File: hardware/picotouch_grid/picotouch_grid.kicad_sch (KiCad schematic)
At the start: 164 parts, among them J1 TRRS, J2 TRRS, J3 TRRS, U1 Pico, U2 TS20, U3 TS20, U5 H11L1

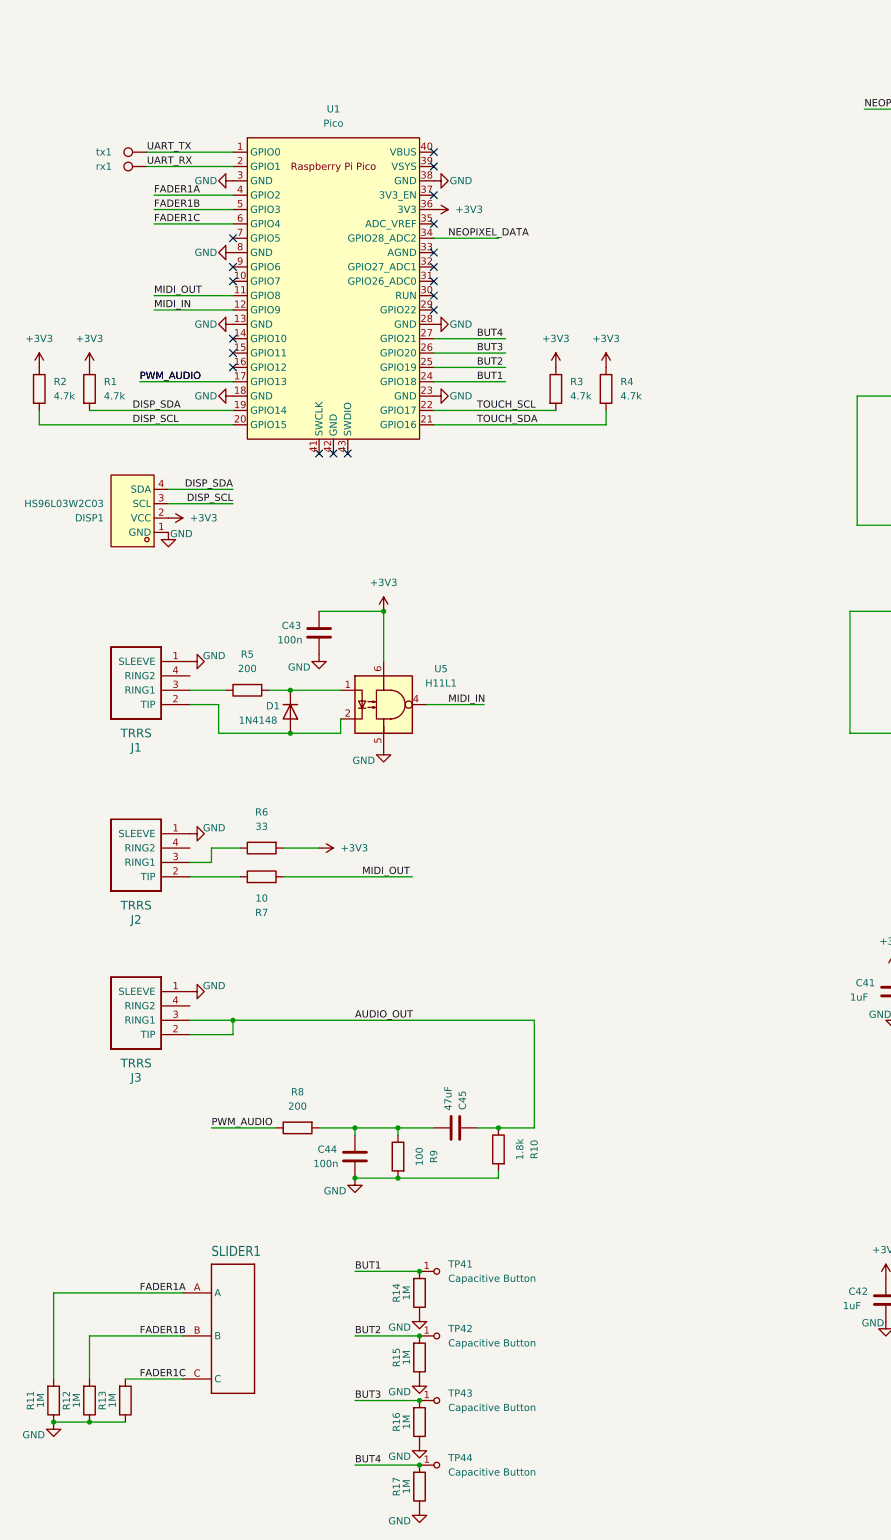
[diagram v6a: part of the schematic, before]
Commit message: pcb: another fader, i2c trace reorg
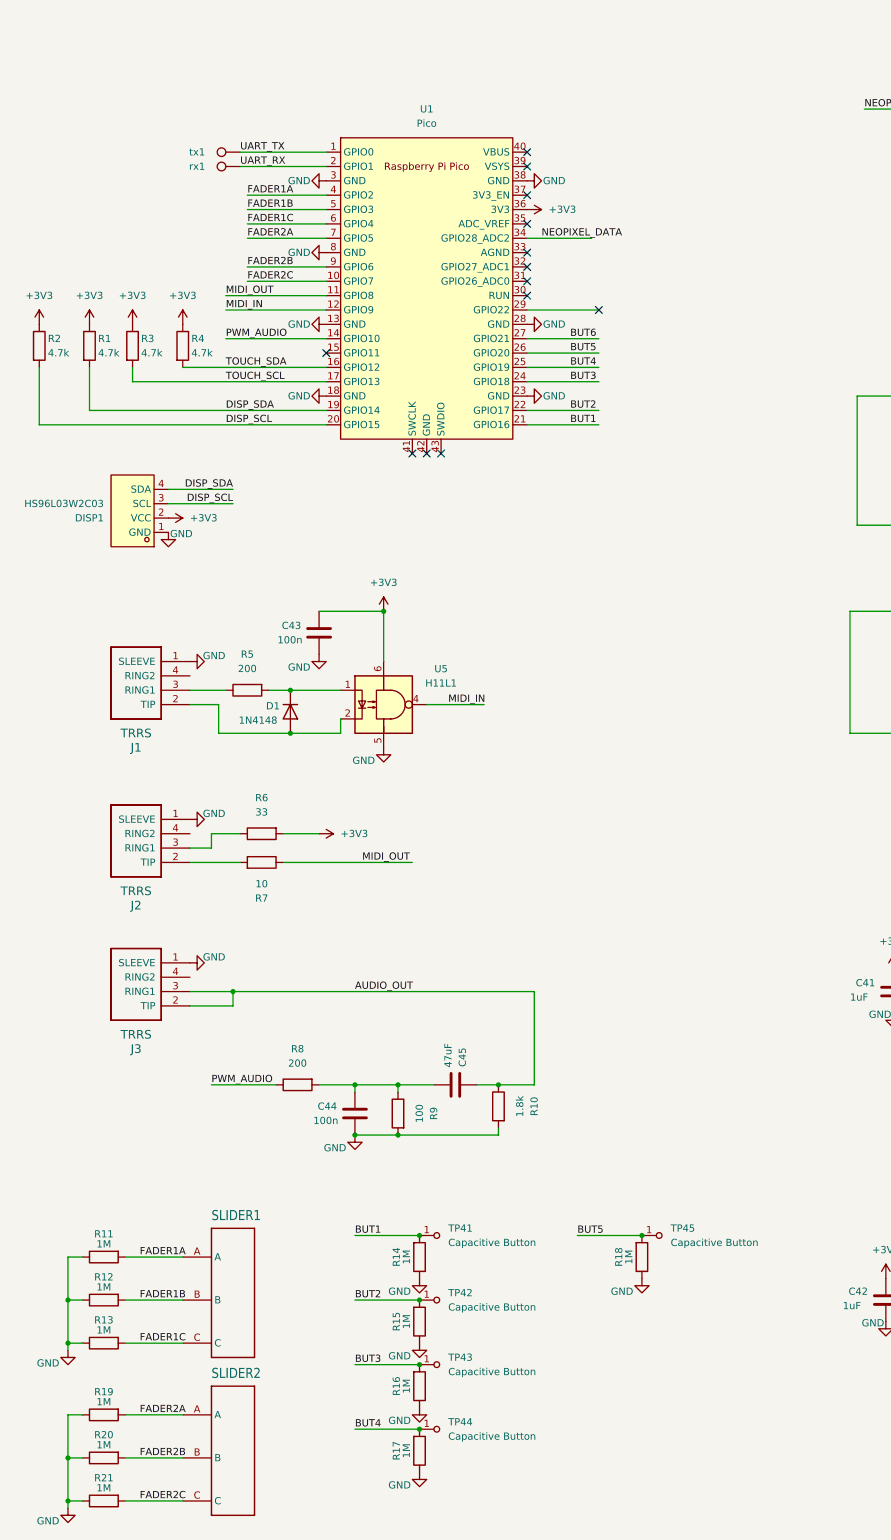
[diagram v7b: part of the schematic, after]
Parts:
- added R18, R19, R20, R21: 1M, Resistor_SMD:R_0603_1608Metric, symbol Device:R
- added SLIDER2: ~, todbot_eagle2023:TOUCHSLIDER3_8x40B, symbol todbot_eagle2023:TouchSlider-3sectors
- added TP45: Capacitive Button, todbot_stuff:Pad-CapacitiveTouch-SparkFun-10x5mm-roundrect, symbol SparkFun-Switch:Capacitive Button
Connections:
- net BUT1: now also U1.21 (GPIO16); no longer U1.24 (GPIO18)
- net BUT2: now also U1.22 (GPIO17); no longer U1.25 (GPIO19)
- net BUT3: now also U1.24 (GPIO18); no longer U1.26 (GPIO20)
- net BUT4: now also U1.25 (GPIO19); no longer U1.27 (GPIO21)
- net GND: now also R18.1, R19.1, R20.1, R21.1
- net PWM_AUDIO: now also U1.14 (GPIO10); no longer U1.17 (GPIO13)
- net TOUCH_SCL: now also U1.17 (GPIO13); no longer U1.22 (GPIO17)
- net TOUCH_SDA: now also U1.16 (GPIO12); no longer U1.21 (GPIO16)
- net FADER2C: now reaches U1.10 (GPIO7)
- net FADER2C: now also R21.2, SLIDER2.C
- net FADER2A: now reaches U1.7 (GPIO5)
- net FADER2A: now also R19.2, SLIDER2.A
- net FADER2B: now reaches U1.9 (GPIO6)
- net FADER2B: now also R20.2, SLIDER2.B
- new net BUT5: R18.2, TP45.1 (A), U1.26 (GPIO20)
- new net BUT6: U1.27 (GPIO21)
- no-connect marks 21 -> 16
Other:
- moved on the sheet: C44, C45, J2, J3, R1, R10, R11, R12, R13, R14, R15, R16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

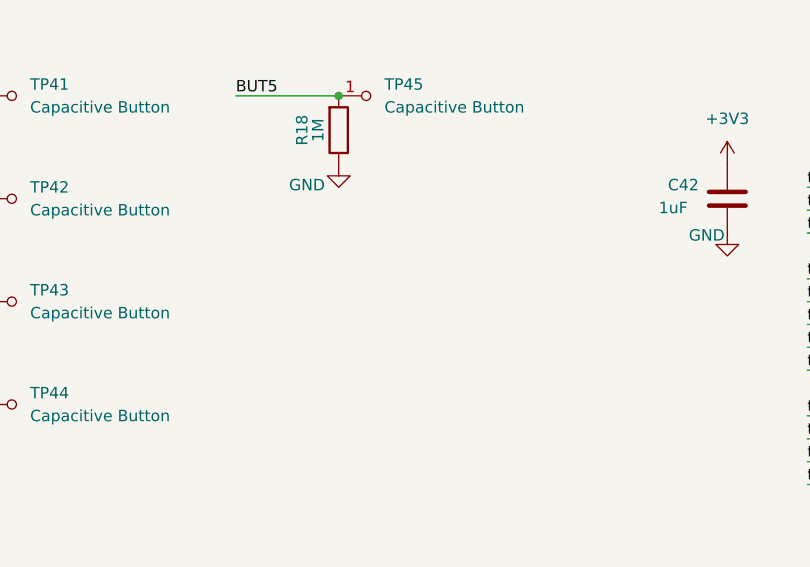
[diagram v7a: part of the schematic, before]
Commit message: pcb: button layout tune
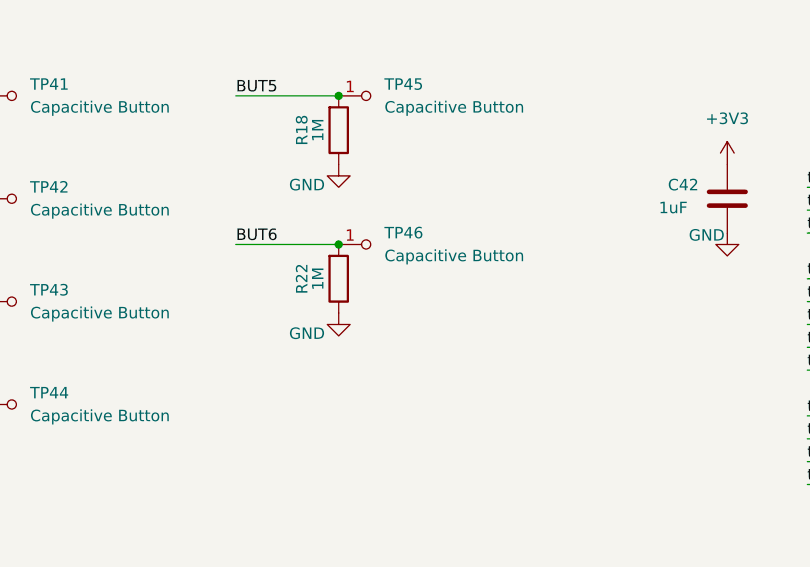
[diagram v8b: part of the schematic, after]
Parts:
- added R22: 1M, Resistor_SMD:R_0603_1608Metric, symbol Device:R
- added TP46: Capacitive Button, todbot_stuff:Pad-CapacitiveTouch-SparkFun-10x5mm-roundrect, symbol SparkFun-Switch:Capacitive Button
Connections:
- net BUT6: now also R22.2, TP46.1 (A)
- net GND: now also R22.1
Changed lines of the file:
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@@
 	)
 	(junction
+		(at 124.46 247.65)
+		(diameter 0)
+		(color 0 0 0 0)
+	)
+	(junction
 		(at 325.12 92.71)
 		(diameter 0)
@@
 	(wire
 		(pts
+			(xy 113.03 247.65) (xy 124.46 247.65)
+		)
+		(stroke
+			(width 0)
+			(type default)
+		)
+	)
+	(wire
+		(pts
 			(xy 271.78 55.88) (xy 279.4 55.88)
 		)
@@
 		)
 	)
+	(label "BUT6"
+		(at 113.03 247.65 0)
+		(fields_autoplaced yes)
+		(effects
+			(font
+				(size 1.27 1.27)
+			)
+			(justify left bottom)
+		)
+	)
 	(label "tp35"
 		(at 367.03 203.2 0)
@@
 	)
 	(symbol
+		(lib_id "power:GND")
+		(at 124.46 255.27 0)
+		(unit 1)
+		(exclude_from_sim no)
+		(in_bom yes)
+		(on_board yes)
+		(dnp no)
+		(property "Reference" "#PWR0164"
+			(at 124.46 261.62 0)
+			(effects
+				(font
+					(size 1.27 1.27)
+				)
+				(hide yes)
+			)
+		)
+		(property "Value" "GND"
+			(at 122.936 257.556 0)
+			(effects
+				(font
+					(size 1.27 1.27)
+				)
+				(justify right)
+			)
+		)
+		(property "Footprint" ""
+			(at 124.46 255.27 0)
+			(effects
+				(font
+					(size 1.27 1.27)
+				)
+				(hide yes)
+			)
+		)
+		(property "Datasheet" ""
+			(at 124.46 255.27 0)
+			(effects
+				(font
+					(size 1.27 1.27)
+				)
+				(hide yes)
+			)
+		)
+		(property "Description" "Power symbol creates a global label with name \"GND\" , ground"
+			(at 124.46 255.27 0)
+			(effects
+				(font
+					(size 1.27 1.27)
+				)
+				(hide yes)
+			)
+		)
+		(pin "1"
+		)
+		(instances
+			(project "picotouch_grid"
+				(path "/036e8f10-ba17-4cdc-95e8-e722ded3fffe"
+					(reference "#PWR0164")
+					(unit 1)
+				)
+			)
+		)
+	)
+	(symbol
 		(lib_id "PCM_marbastlib-various:SK6812MINI-E")
 		(at 325.12 31.75 0)
@@
 	(symbol
 		(lib_id "Device:R")
+		(at 124.46 251.46 0)
+		(mirror x)
+		(unit 1)
+		(exclude_from_sim no)
+		(in_bom yes)
+		(on_board yes)
+		(dnp no)
+		(property "Reference" "R22"
+			(at 120.396 251.46 90)
+			(effects
+				(font
+					(size 1.27 1.27)
+				)
+			)
+		)
+		(property "Value" "1M"
+			(at 122.174 251.46 90)
+			(effects
+				(font
+					(size 1.27 1.27)
+				)
+			)
+		)
+		(property "Footprint" "Resistor_SMD:R_0603_1608Metric"
+			(at 122.682 251.46 90)
+			(effects
+				(font
+					(size 1.27 1.27)
+				)
+				(hide yes)
+			)
+		)
+		(property "Datasheet" "~"
+			(at 124.46 251.46 0)
+			(effects
+				(font
+					(size 1.27 1.27)
+				)
+				(hide yes)
+			)
+		)
+		(property "Description" "Resistor"
+			(at 124.46 251.46 0)
+			(effects
+				(font
+					(size 1.27 1.27)
+				)
+				(hide yes)
+			)
+		)
+		(pin "2"
+		)
+		(pin "1"
+		)
+		(instances
+			(project "picotouch_grid"
+				(path "/036e8f10-ba17-4cdc-95e8-e722ded3fffe"
+					(reference "R22")
+					(unit 1)
+				)
+			)
+		)
+	)
+	(symbol
+		(lib_id "Device:R")
 		(at 124.46 234.95 0)
 		(mirror x)
@@
 					(unit 1)
 				)
+			)
+		)
+	)
+	(symbol
+		(lib_id "SparkFun-Switch:Capacitive Button")
+		(at 124.46 247.65 270)
+		(unit 1)
+		(exclude_from_sim no)
+		(in_bom yes)
+		(on_board yes)
+		(dnp no)
+		(fields_autoplaced yes)
+		(property "Reference" "TP46"
+			(at 129.54 246.3799 90)
+			(effects
+				(font
+					(size 1.27 1.27)
+				)
+				(justify left)
+			)
+		)
+		(property "Value" "Capacitive Button"
+			(at 129.54 248.9199 90)
+			(effects
+				(font
+					(size 1.27 1.27)
+				)
+				(justify left)
+			)
+		)
+		(property "Footprint" "todbot_stuff:Pad-CapacitiveTouch-SparkFun-10x5mm-roundrect"
+			(at 116.84 247.65 0)
+			(effects
+				(font
+					(size 1.27 1.27)
+				)
+				(hide yes)
+			)
+		)
+		(property "Datasheet" "~"
+			(at 114.3 247.65 0)
+			(effects
+				(font
+					(size 1.27 1.27)
+				)
+				(hide yes)
+			)
+		)
+		(property "Description" "Single Pole Single Throw (SPST) switch"
+			(at 124.46 247.65 0)
+			(effects
+				(font
+					(size 1.27 1.27)
+				)
+				(hide yes)
+			)
+		)
+		(pin "1"
+		)
+		(instances
+			(project "picotouch_grid"
+				(path "/036e8f10-ba17-4cdc-95e8-e722ded3fffe"
+					(reference "TP46")
+					(unit 1)
+				)
